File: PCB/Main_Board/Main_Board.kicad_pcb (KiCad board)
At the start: 2 copper layers, 68.2 x 58.2 mm, 62 parts, among them IC1 74LV1T34GVH, J1 USB_B_Micro, J2 Screw_Terminal_01x02, J3 SJ1-3523N, J4 SJ1-3523N, J5 Screw_Terminal_01x04, J6 Screw_Terminal_01x06, Q1 MBT3904DW1, SW1 SW_SPDT, SW2 EN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

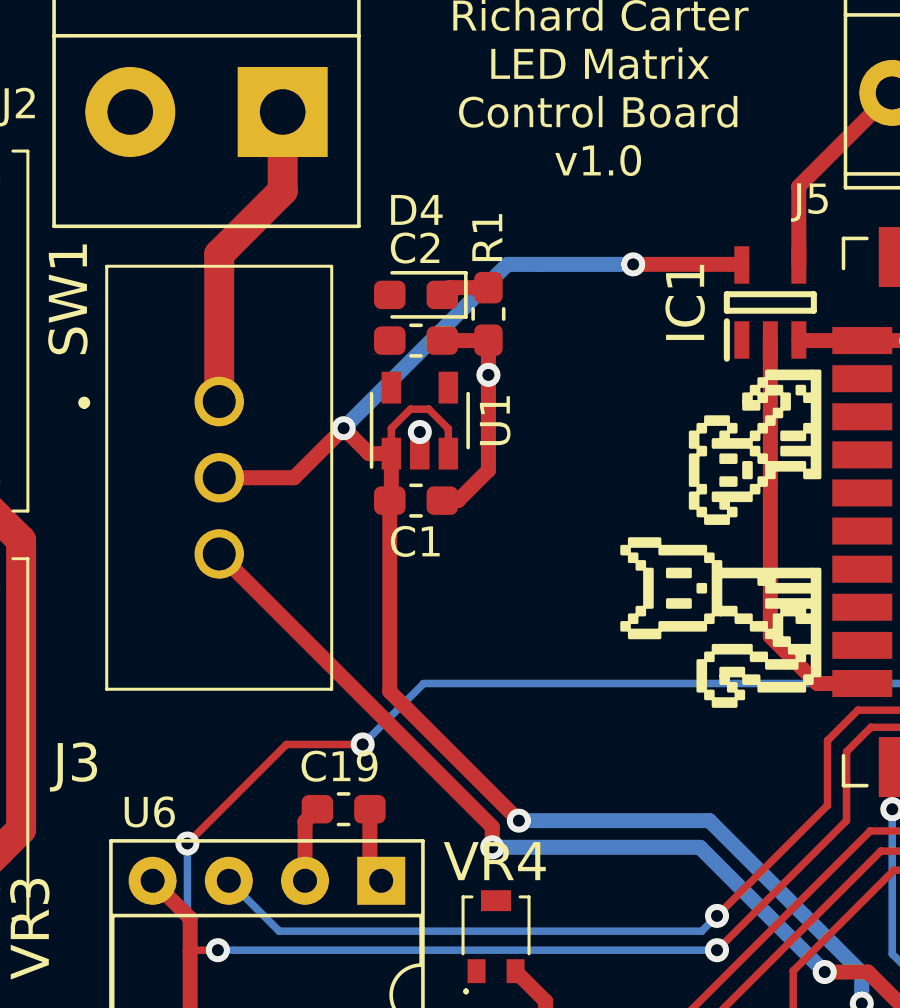
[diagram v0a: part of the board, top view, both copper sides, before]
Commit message: Move indicator LED to 5V and increase indicator LED resistors
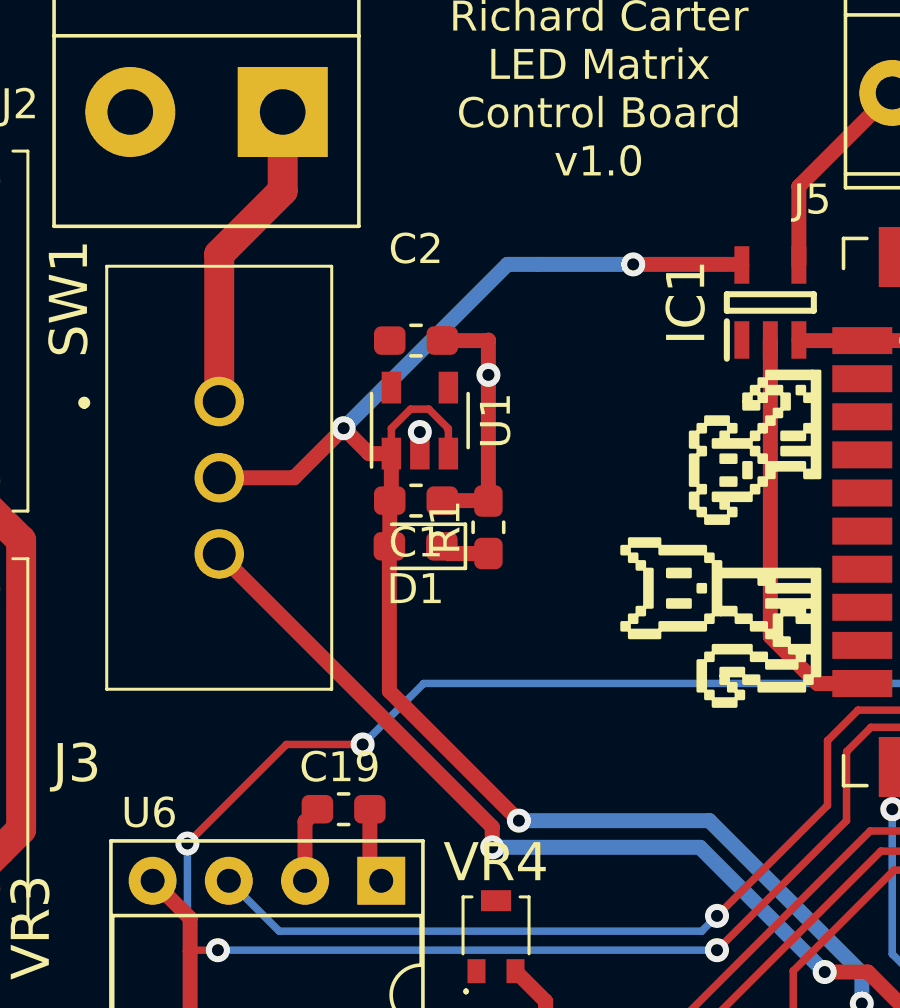
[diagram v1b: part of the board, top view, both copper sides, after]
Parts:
- removed D4: 3V3_LED, LED_SMD:LED_0603_1608Metric_Pad1.05x0.95mm_HandSolder
- added D1: 5V_LED, LED_SMD:LED_0603_1608Metric_Pad1.05x0.95mm_HandSolder, F.Cu at (77.8, 135.8)
- R1: value CUR_LIMIT_5.6R -> CUR_LIMIT_220R
- R7, R8: value CUR_LIMIT_100R -> CUR_LIMIT_220R
- moved R1 7.11 mm to (80.3, 135.1), turned to 90 degrees
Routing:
- net Earth: track 82.3 -> 82.9 mm
